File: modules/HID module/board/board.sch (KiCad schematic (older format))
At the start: 30 parts, among them J1 USB_C_Receptacle_USB2.0, J2 Conn_01x06, J3 Conn_01x06, J6 Conn_01x06, SW1 RESET, U1 ESP32-WROOM-32, U2 HT7533-1-SOT89, U3 HT42B564

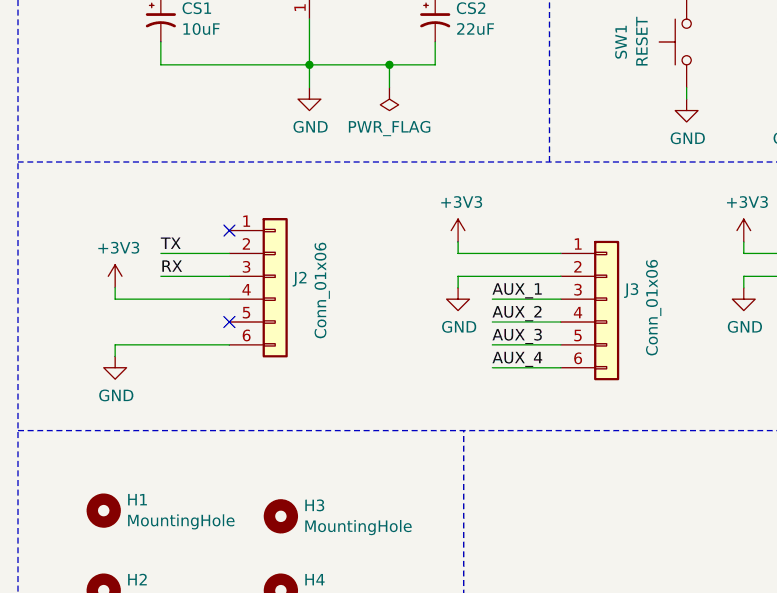
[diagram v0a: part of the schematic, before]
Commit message: PCB: USB C receptacle moved close to PCB edge
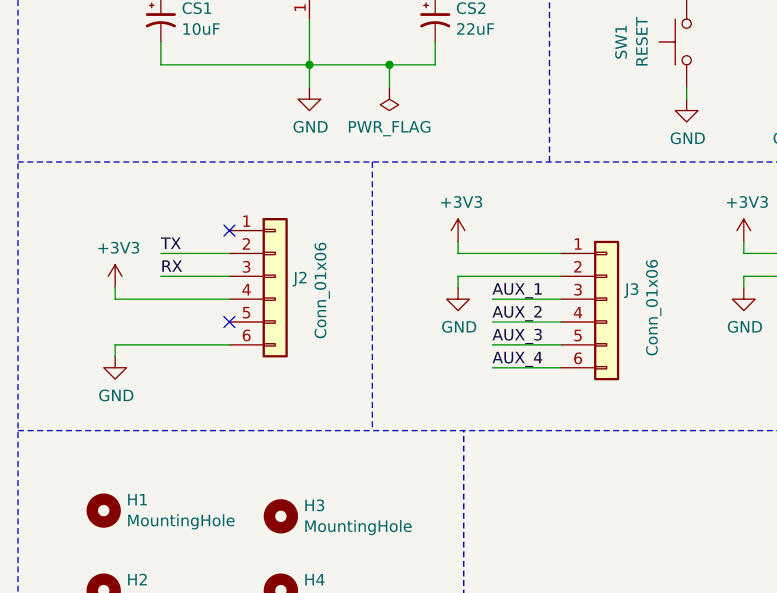
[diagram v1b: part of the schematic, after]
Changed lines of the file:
@@
 Text Label 8075 2900 2    50   ~ 0
 LED_P
+Wire Notes Line
+	3300 4825 3300 6000
 $EndSCHEMATC
